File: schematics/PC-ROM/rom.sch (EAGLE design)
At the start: 9 parts

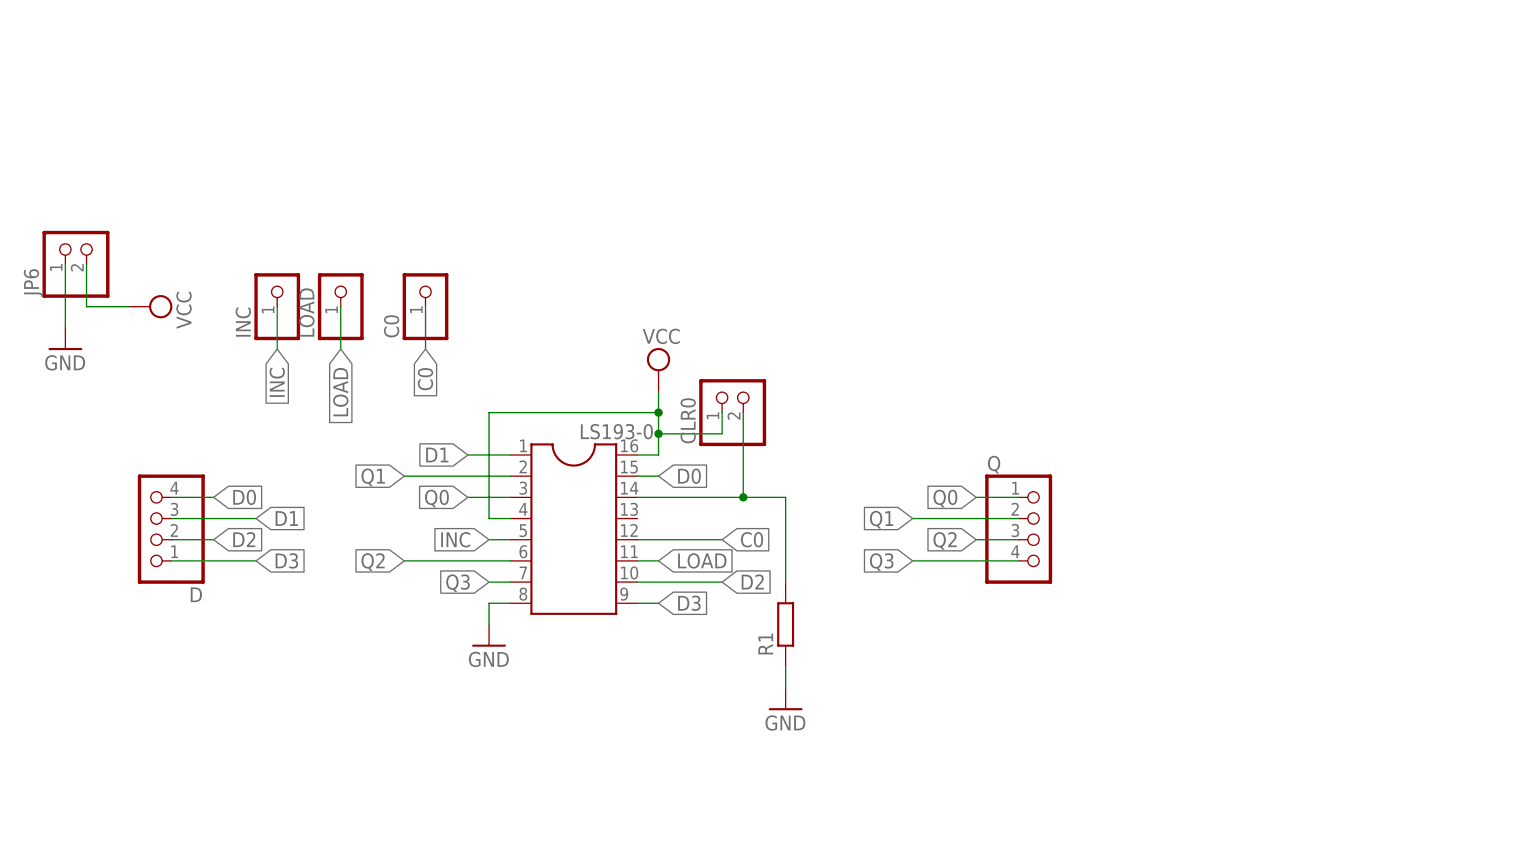
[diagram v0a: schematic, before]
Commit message: Added sch, brd and gerber file for register, register bus, pc and ROM.
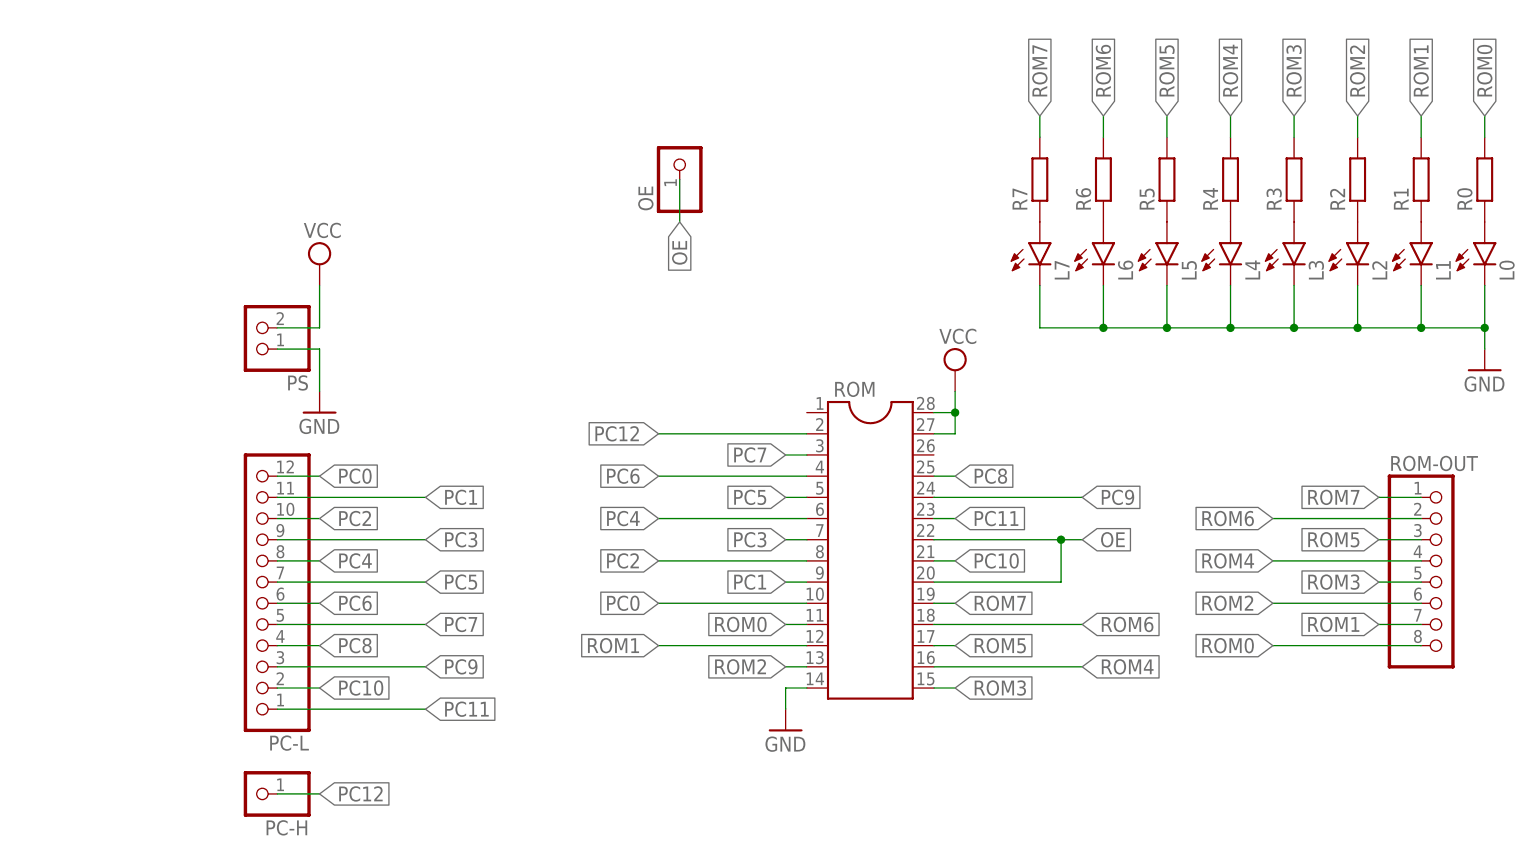
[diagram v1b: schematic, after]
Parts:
- removed C0, INC, LOAD: (no value), pinhead:PINHD-1X1
- removed CLR0, JP6: (no value), pinhead:PINHD-1X2
- removed D, Q: (no value), pinhead:PINHD-1X4
- removed LS193-0: (no value), ic-package:DIL16S
- added L0, L1, L2, L3, L4, L5, L6, L7: (no value), led:LED5MM
- added OE, PC-H: (no value), pinhead:PINHD-1X1
- added PC-L: (no value), pinhead:PINHD-1X12
- added PS: (no value), pinhead:PINHD-1X2
- added R0, R2, R3, R4, R5, R6, R7: (no value), rcl:R-EU_0204/7
- added ROM: (no value), ic-package:DIL28
- added ROM-OUT: (no value), pinhead:PINHD-1X8
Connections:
- removed net C0: C0.1, LS193-0.12
- removed net CLR-0: CLR0.2, LS193-0.14, R1.2
- removed net D0: D.4, LS193-0.15
- removed net D1: D.3, LS193-0.1
- removed net D2: D.2, LS193-0.10
- removed net D3: D.1, LS193-0.9
- removed net INC: INC.1, LS193-0.5
- removed net LOAD: LOAD.1, LS193-0.11
- removed net Q0: LS193-0.3, Q.1
- removed net Q1: LS193-0.2, Q.2
- removed net Q2: LS193-0.6, Q.3
- removed net Q3: LS193-0.7, Q.4
- new net N$1: L7.A, R7.1
- new net N$2: L6.A, R6.1
- new net N$3: L5.A, R5.1
- new net N$4: L4.A, R4.1
- new net N$5: L3.A, R3.1
- new net N$6: L2.A, R2.1
- new net N$7: L1.A, R1.1
- new net N$8: L0.A, R0.1
- new net OE: OE.1, ROM.20, ROM.22
- new net PC0: PC-L.12, ROM.10
- new net PC1: PC-L.11, ROM.9
- new net PC10: PC-L.2, ROM.21
- new net PC11: PC-L.1, ROM.23
- new net PC12: PC-H.1, ROM.2
- new net PC2: PC-L.10, ROM.8
- new net PC3: PC-L.9, ROM.7
- new net PC4: PC-L.8, ROM.6
- new net PC5: PC-L.7, ROM.5
- new net PC6: PC-L.6, ROM.4
- new net PC7: PC-L.5, ROM.3
- new net PC8: PC-L.4, ROM.25
- new net PC9: PC-L.3, ROM.24
- new net ROM0: R0.2, ROM-OUT.8, ROM.11
- new net ROM1: R1.2, ROM-OUT.7, ROM.12
- new net ROM2: R2.2, ROM-OUT.6, ROM.13
- new net ROM3: R3.2, ROM-OUT.5, ROM.15
- new net ROM4: R4.2, ROM-OUT.4, ROM.16
- new net ROM5: R5.2, ROM-OUT.3, ROM.17
- new net ROM6: R6.2, ROM-OUT.2, ROM.18
- new net ROM7: R7.2, ROM-OUT.1, ROM.19
- net GND: now also L0.C, L1.C, L2.C, L3.C, L4.C, L5.C, L6.C, L7.C, PS.1, ROM.14; no longer JP6.1, LS193-0.8, R1.1
- net VCC: now also PS.2, ROM.27, ROM.28; no longer CLR0.1, JP6.2, LS193-0.16, LS193-0.4
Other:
- moved on the sheet: R1
